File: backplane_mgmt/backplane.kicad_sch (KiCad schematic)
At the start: 5 parts, among them J201 Backplane, U203 AT24CS32-SSHM

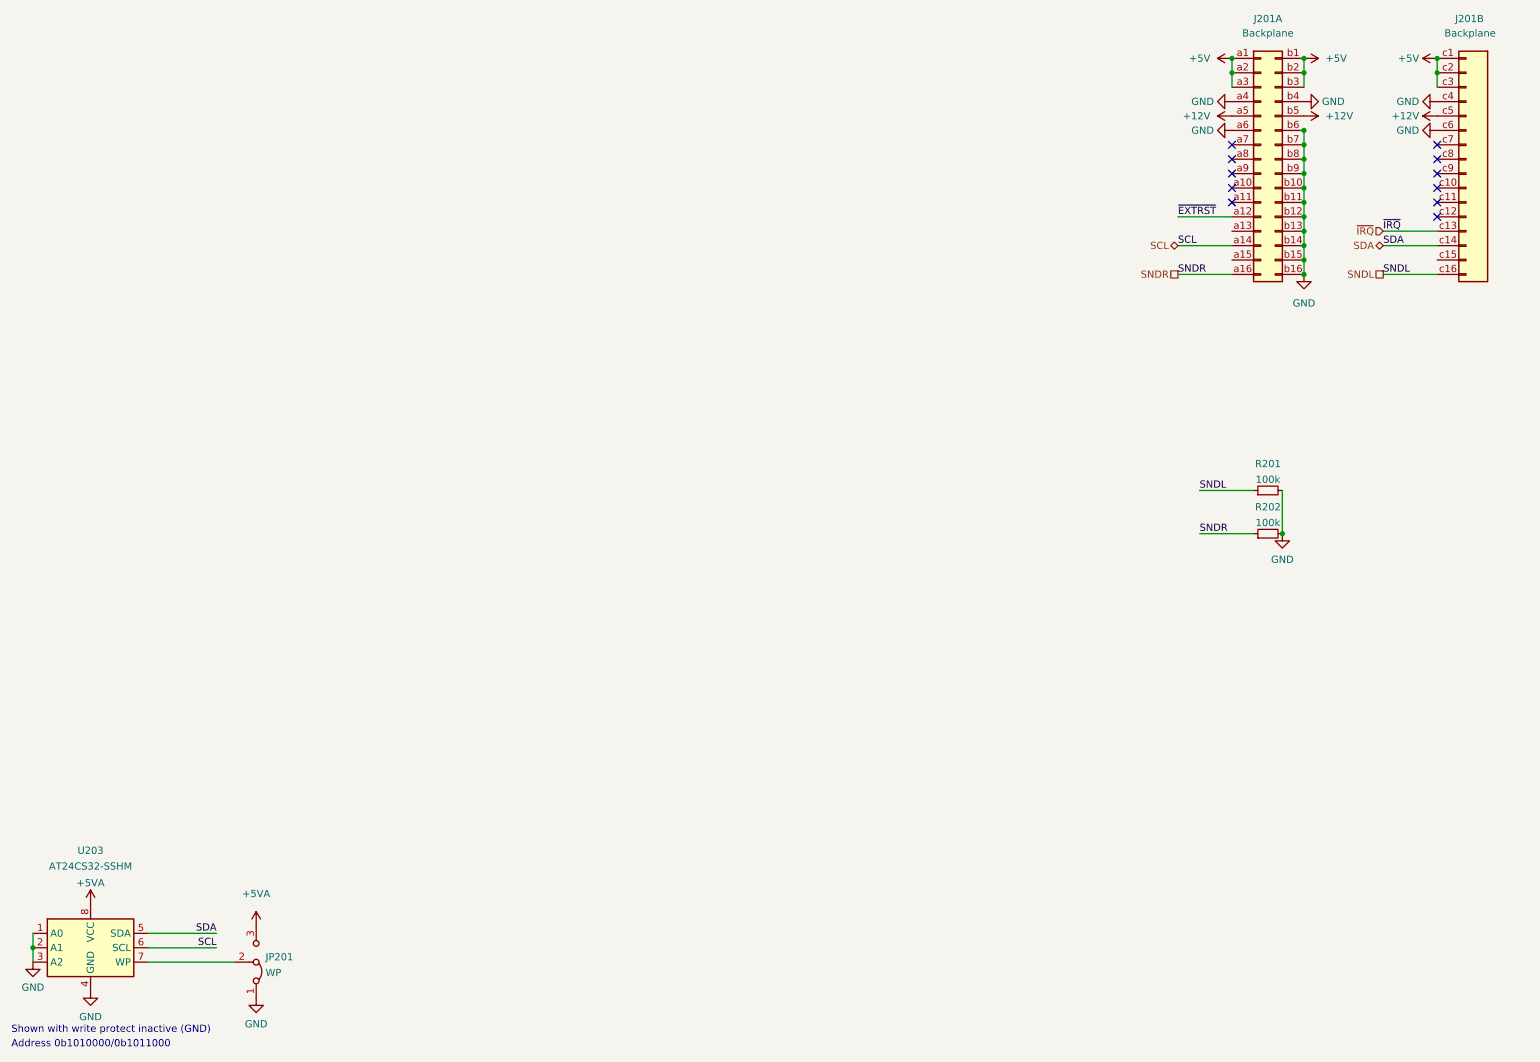
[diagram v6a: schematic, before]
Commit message: Minor tweaks based from assembly
- Replaced the AT24CS32 EEPROMs with the AT24CS16 which is what was
  ordered. These are half the size, but use a totally different
  addressing scheme which needs to be followed. So, we should just
  standardize on these.

  The information stored in the actual EEPROM section (2KBytes in this
  part) will likely not be much larger than a small 32 byte (or so)
  header.

- Removed a few redundant parts on the power management board, namely
  some resistors

- Fixed the fucked footprint for the PTH08T220WAD module; the annular
  rings were way too small
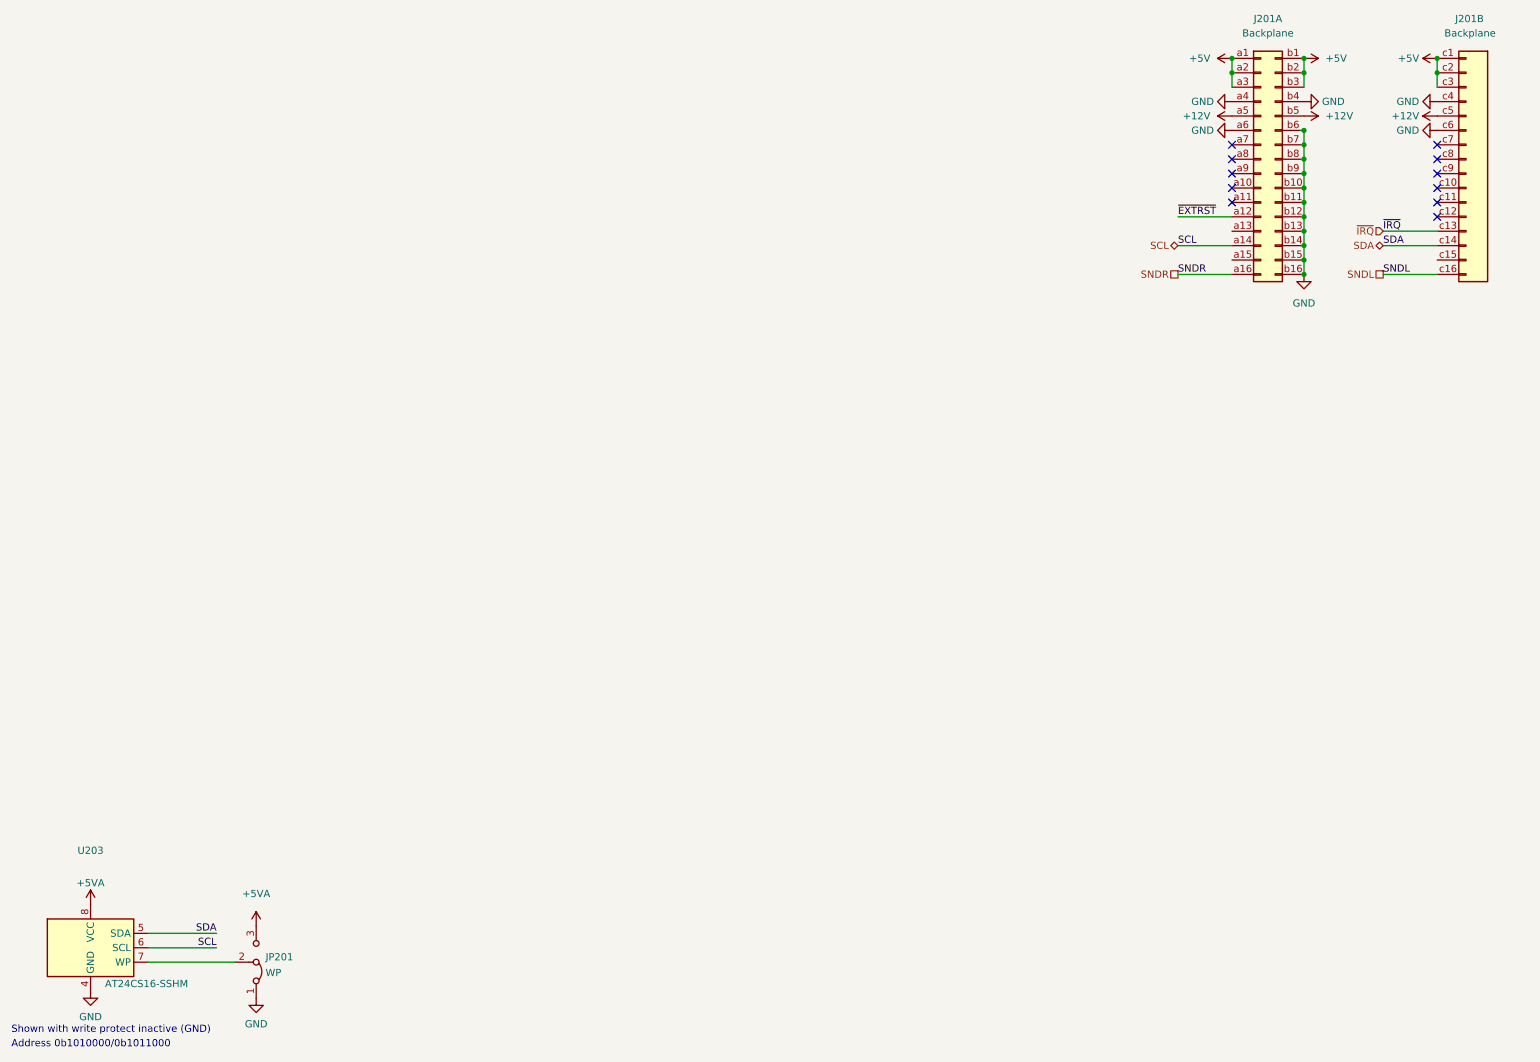
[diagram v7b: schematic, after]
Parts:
- removed R201, R202: 100k, Resistor_SMD:R_0805_2012Metric, symbol Device:R_Small
- U203: value AT24CS32-SSHM -> AT24CS16-SSHM; symbol Memory_EEPROM:AT24CS32-SSHM -> Memory_EEPROM:AT24CS16-SSHM
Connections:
- net GND: no longer U203.1 (A0), U203.2 (A1), U203.3 (A2)
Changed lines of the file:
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@@
   (title_block
     (title "Backplane Management and Power")
-    (date "2022-01-23")
-    (rev "1")
+    (date "2022-03-02")
+    (rev "2")
     (company "Tristan Seifert")
   )
-  (junction (at 241.3 105.41) (diameter 0) (color 0 0 0 0)
-  )
   (junction (at 245.11 24.13) (diameter 0) (color 0 0 0 0)
   )
@@
   )
   (junction (at 245.11 59.69) (diameter 0) (color 0 0 0 0)
-  )
-  (junction (at 20.955 178.435) (diameter 0) (color 0 0 0 0)
   )
   (no_connect (at 232.41 46.99))
@@
     (stroke (width 0) (type default) (color 0 0 0 0))
   )
-  (wire (pts (xy 20.955 175.895) (xy 20.955 178.435))
-    (stroke (width 0) (type default) (color 0 0 0 0))
-  )
   (wire (pts (xy 41.275 178.435) (xy 53.34 178.435))
     (stroke (width 0) (type default) (color 0 0 0 0))
@@
     (stroke (width 0) (type default) (color 0 0 0 0))
   )
-  (wire (pts (xy 226.695 97.79) (xy 236.22 97.79))
-    (stroke (width 0) (type default) (color 0 0 0 0))
-  )
   (wire (pts (xy 41.275 180.975) (xy 56.515 180.975))
     (stroke (width 0) (type default) (color 0 0 0 0))
   )
-  (wire (pts (xy 226.695 105.41) (xy 236.22 105.41))
-    (stroke (width 0) (type default) (color 0 0 0 0))
-  )
-  (wire (pts (xy 241.3 97.79) (xy 241.3 105.41))
-    (stroke (width 0) (type default) (color 0 0 0 0))
-  )
   (wire (pts (xy 259.08 54.61) (xy 268.605 54.61))
     (stroke (width 0) (type default) (color 0 0 0 0))
@@
   )
   (wire (pts (xy 245.11 24.13) (xy 245.11 26.67))
-    (stroke (width 0) (type default) (color 0 0 0 0))
-  )
-  (wire (pts (xy 20.955 178.435) (xy 20.955 180.975))
     (stroke (width 0) (type default) (color 0 0 0 0))
   )
@@
     (effects (font (size 1.27 1.27)) (justify left bottom))
   )
-  (label "SNDL" (at 226.695 97.79 0)
-    (effects (font (size 1.27 1.27)) (justify left bottom))
-  )
-  (label "SNDR" (at 226.695 105.41 0)
-    (effects (font (size 1.27 1.27)) (justify left bottom))
-  )
   (label "SNDR" (at 222.885 59.69 0)
     (effects (font (size 1.27 1.27)) (justify left bottom))
@@
     (pin "1")
   )
-  (symbol (lib_id "power:GND") (at 20.955 180.975 0) (unit 1)
-    (in_bom yes) (on_board yes) (fields_autoplaced)
-    (property "Reference" "#PWR0222" (id 0) (at 20.955 187.325 0)
-      (effects (font (size 1.27 1.27)) hide)
-    )
-    (property "Value" "GND" (id 1) (at 20.955 185.42 0))
-    (property "Footprint" "" (id 2) (at 20.955 180.975 0)
-      (effects (font (size 1.27 1.27)) hide)
-    )
-    (property "Datasheet" "" (id 3) (at 20.955 180.975 0)
-      (effects (font (size 1.27 1.27)) hide)
-    )
-    (pin "1")
-  )
   (symbol (lib_id "power:+12V") (at 245.11 31.75 270) (unit 1)
     (in_bom yes) (on_board yes) (fields_autoplaced)
@@
     )
     (property "Datasheet" "" (id 3) (at 245.11 21.59 0)
-      (effects (font (size 1.27 1.27)) hide)
-    )
-    (pin "1")
-  )
-  (symbol (lib_id "power:GND") (at 241.3 105.41 0) (unit 1)
-    (in_bom yes) (on_board yes) (fields_autoplaced)
-    (property "Reference" "#PWR0110" (id 0) (at 241.3 111.76 0)
-      (effects (font (size 1.27 1.27)) hide)
-    )
-    (property "Value" "GND" (id 1) (at 241.3 109.9725 0))
-    (property "Footprint" "" (id 2) (at 241.3 105.41 0)
-      (effects (font (size 1.27 1.27)) hide)
-    )
-    (property "Datasheet" "" (id 3) (at 241.3 105.41 0)
       (effects (font (size 1.27 1.27)) hide)
     )
@@
     (pin "1")
   )
-  (symbol (lib_id "Memory_EEPROM:AT24CS32-SSHM") (at 31.115 178.435 0) (unit 1)
+  (symbol (lib_id "Memory_EEPROM:AT24CS16-SSHM") (at 31.115 178.435 0) (unit 1)
     (in_bom yes) (on_board yes)
     (property "Reference" "U203" (id 0) (at 31.115 161.29 0))
-    (property "Value" "AT24CS32-SSHM" (id 1) (at 31.115 164.0651 0))
+    (property "Value" "AT24CS16-SSHM" (id 1) (at 33.655 184.785 0)
+      (effects (font (size 1.27 1.27)) (justify left))
+    )
     (property "Footprint" "Package_SO:SOIC-8_3.9x4.9mm_P1.27mm" (id 2) (at 31.115 178.435 0)
       (effects (font (size 1.27 1.27)) hide)
     )
-    (property "Datasheet" "http://ww1.microchip.com/downloads/en/DeviceDoc/Atmel-8869-SEEPROM-AT24CS32-Datasheet.pdf" (id 3) (at 31.115 178.435 0)
+    (property "Datasheet" "http://ww1.microchip.com/downloads/en/DeviceDoc/Atmel-8859-SEEPROM-AT24CS16-Datasheet.pdf" (id 3) (at 31.115 178.435 0)
       (effects (font (size 1.27 1.27)) hide)
     )
@@
       (effects (font (size 1.27 1.27)) hide)
     )
-    (pin "1")
-    (pin "2")
-    (pin "3")
     (pin "4")
     (pin "5")
@@
     (pin "8")
   )
-  (symbol (lib_id "Device:R_Small") (at 238.76 105.41 90) (unit 1)
-    (in_bom yes) (on_board yes) (fields_autoplaced)
-    (property "Reference" "R202" (id 0) (at 238.76 100.7069 90))
-    (property "Value" "100k" (id 1) (at 238.76 103.482 90))
-    (property "Footprint" "Resistor_SMD:R_0805_2012Metric" (id 2) (at 238.76 105.41 0)
-      (effects (font (size 1.27 1.27)) hide)
-    )
-    (property "Datasheet" "~" (id 3) (at 238.76 105.41 0)
-      (effects (font (size 1.27 1.27)) hide)
-    )
-    (pin "1")
-    (pin "2")
-  )
   (symbol (lib_id "power:GND") (at 268.605 34.29 270) (unit 1)
     (in_bom yes) (on_board yes) (fields_autoplaced)
@@
     (pin "3")
   )
-  (symbol (lib_id "Device:R_Small") (at 238.76 97.79 90) (unit 1)
-    (in_bom yes) (on_board yes) (fields_autoplaced)
-    (property "Reference" "R201" (id 0) (at 238.76 93.0869 90))
-    (property "Value" "100k" (id 1) (at 238.76 95.862 90))
-    (property "Footprint" "Resistor_SMD:R_0805_2012Metric" (id 2) (at 238.76 97.79 0)
-      (effects (font (size 1.27 1.27)) hide)
-    )
-    (property "Datasheet" "~" (id 3) (at 238.76 97.79 0)
-      (effects (font (size 1.27 1.27)) hide)
-    )
-    (pin "1")
-    (pin "2")
-  )
   (symbol (lib_id "power:GND") (at 31.115 186.055 0) (unit 1)
